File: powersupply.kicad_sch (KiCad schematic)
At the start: 25 parts, among them J4 USB_C_Receptacle_USB2.0_16P, J8 Conn_01x02_Pin, U2 AMS1117-3.3, U3 DW01A, U6 TP4056

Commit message: wip schematic
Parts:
- removed C6: 4u7, Capacitor_SMD:C_0603_1608Metric, symbol Capacitor_E12_0603:Capacitor_820n
- added C6: 100n, Capacitor_SMD:C_0603_1608Metric, symbol _PS_LIB:C_0603
- added Q1: Dual_NMOS_8205A, Package_TO_SOT_SMD:SOT-23-6, symbol _PS_LIB:Dual_NMOS_8205A
- added R20, R21: 100K, Resistor_SMD:R_0603_1608Metric, symbol Resistor_E12_0603:Resistor 100K
- D5: value LED -> LED Rot
- U3: LCSC (none) -> C2927799
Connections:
- net GND: now also C13.2, R8.2, C6.2, Q1.3 (S), R21.2
- net USB5V: now also C6.1
- net battery+: now also R20.1
- net battery-: now also Q1.1 (S); no longer C13.2
- net READY: now reaches R19.2, U6.6 (STAT2)
- net CHARGING: now reaches R18.2, U6.7 (STAT1)
- net at U3.1 (OD): now also Q1.6 (G)
- net at U3.2 (CS): now also R8.1
- net at U3.3 (OC): now also Q1.4 (G)
- new net: Q1.2 (D), Q1.5 (D)
- new net UBAT: R20.2, R21.1
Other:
- note removed: "Tiefentladeschutz einbauen"
- moved on the sheet: C9, J8, R7, R8, U3

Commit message: wip - schematic and layout
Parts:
- added C14: 100n, Capacitor_SMD:C_0603_1608Metric, symbol _PS_LIB:C_0603
- added U7: XC6206P182MR, Package_TO_SOT_SMD:TSOT-23, symbol Regulator_Linear:AP2127N3-1.2
- J8: footprint TerminalBlock_Phoenix:TerminalBlock_Phoenix_MKDS-1-2-3.81_1x02_P3.81mm_Horizontal -> Connector_PinHeader_2.00mm:PinHeader_1x02_P2.00mm_Vertical
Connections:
- net +3.3V: now also U7.3 (VI)
- net GND: now also C14.2, U7.1 (GND)
- new net +1.8V: C14.1, U7.2 (VO)
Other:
- note added: "Vape Battery: 37x17mm"

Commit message: wip
lcsc part numbers
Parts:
- removed C13: 4u7, Capacitor_SMD:C_0603_1608Metric, symbol Capacitor_E12_0603:Capacitor_820n
- removed U7: XC6206P182MR, Package_TO_SOT_SMD:TSOT-23, symbol Regulator_Linear:AP2127N3-1.2
- added C17: 10u 10V, Capacitor_SMD:C_0603_1608Metric, symbol _PS_LIB:C_0603
- added U9: XC6220B181MR, Package_TO_SOT_SMD:SOT-23-5, symbol Regulator_Linear:LP2985-1.8
- C1, C2: value 10u 25V -> 10u 10V; LCSC (none) -> C2959727
- D1, D3, D4: LCSC (none) -> C383211
- D2, D8: LCSC (none) -> C2939001
- D5: LCSC (none) -> C965799
- J4: LCSC (none) -> C2988369
- R1, R2, R3: LCSC (none) -> C431786
- U2: LCSC (none) -> C347222
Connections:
- net +1.8V: now also U9.5 (VOUT)
- net +3.3V: now also U9.1 (VIN)
- net GND: now also C17.2, U9.2 (GND)
- net battery+: now also C17.1
- new net SHDN1: U9.3 (ON/~{OFF})
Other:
- moved on the sheet: C14

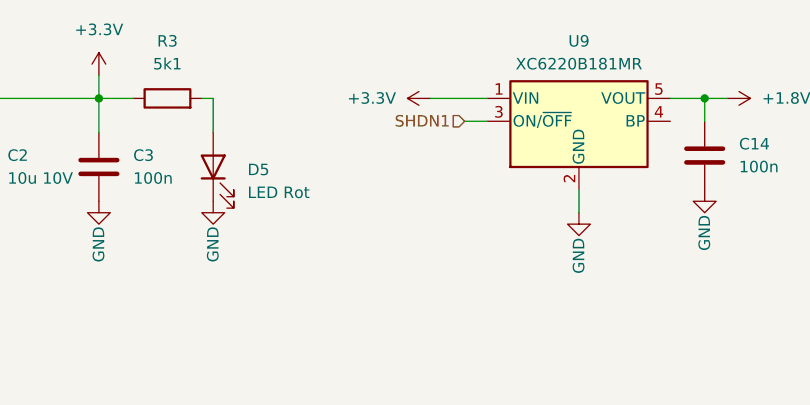
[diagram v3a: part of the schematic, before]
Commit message: level shift for op en added
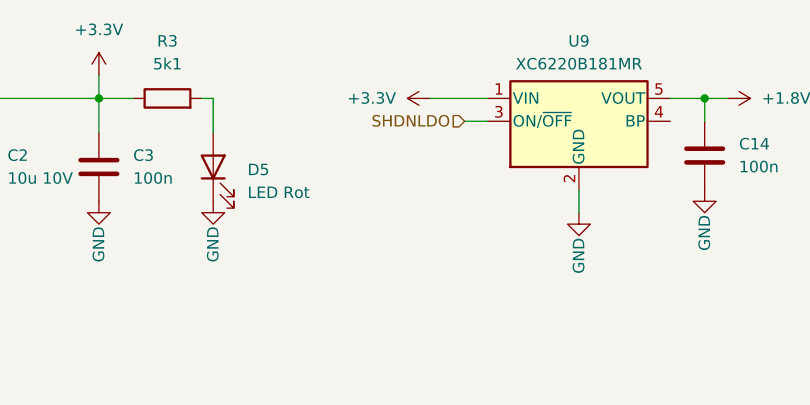
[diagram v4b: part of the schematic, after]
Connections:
- net SHDN1 renamed SHDNLDO
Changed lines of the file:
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@@
+		)
+	)
+	(hierarchical_label "SHDNLDO"
+		(shape input)
+		(at 200.66 40.64 180)
+		(effects
+			(font
+				(size 1.27 1.27)
+			)
+			(justify right)
 		)
 	)
@@
 		)
 	)
-	(hierarchical_label "SHDN1"
-		(shape input)
-		(at 200.66 40.64 180)
-		(effects
-			(font
-				(size 1.27 1.27)
-			)
-			(justify right)
-		)
-	)
